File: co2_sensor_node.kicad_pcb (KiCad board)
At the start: 4 copper layers, 83 parts, among them J1 Conn_01x03, J10 Conn_01x05, J11 Conn_01x06_Male, J12 Conn_01x02, J13 TF-15x15, J2 Conn_01x03, J3 Conn_01x02, J4 Conn_01x02, J5 Conn_01x03, J6 Conn_01x03, J7 Conn_01x02, J8 Conn_01x03, J9 Conn_01x05, Q1 AO3400A, Q2 AO3401A, Q3 AO3401A, Q4 AO3400A, SW1 K2-1102SP-C4SC-04, U1 TPS62130, U2 ESP32-WROOM-32D, U3 TC1508S

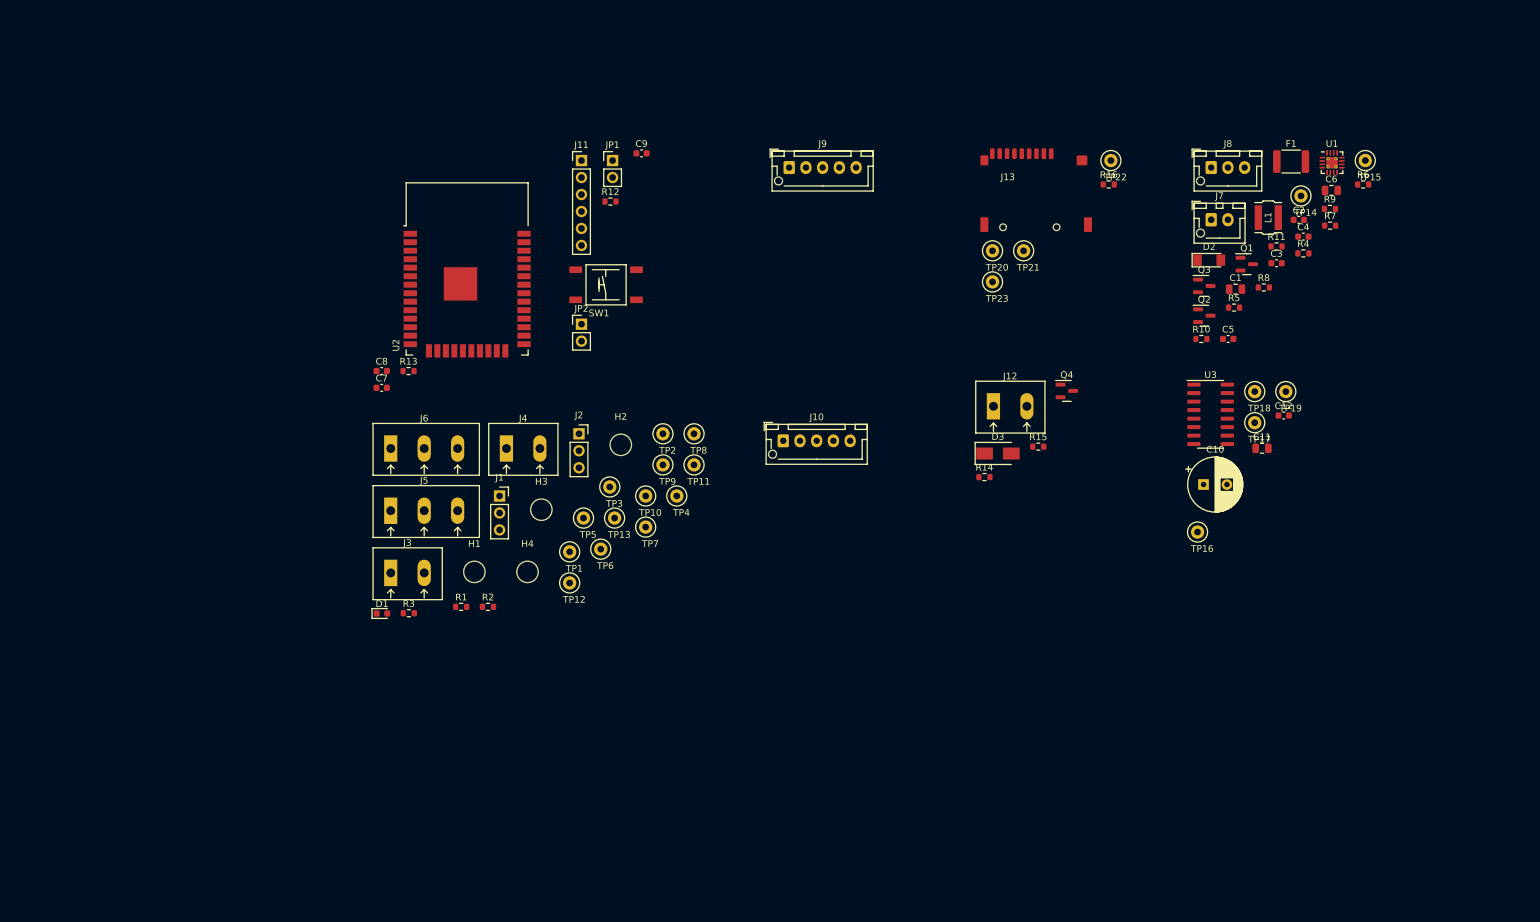
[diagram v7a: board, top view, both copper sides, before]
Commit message: Finish PCB layout
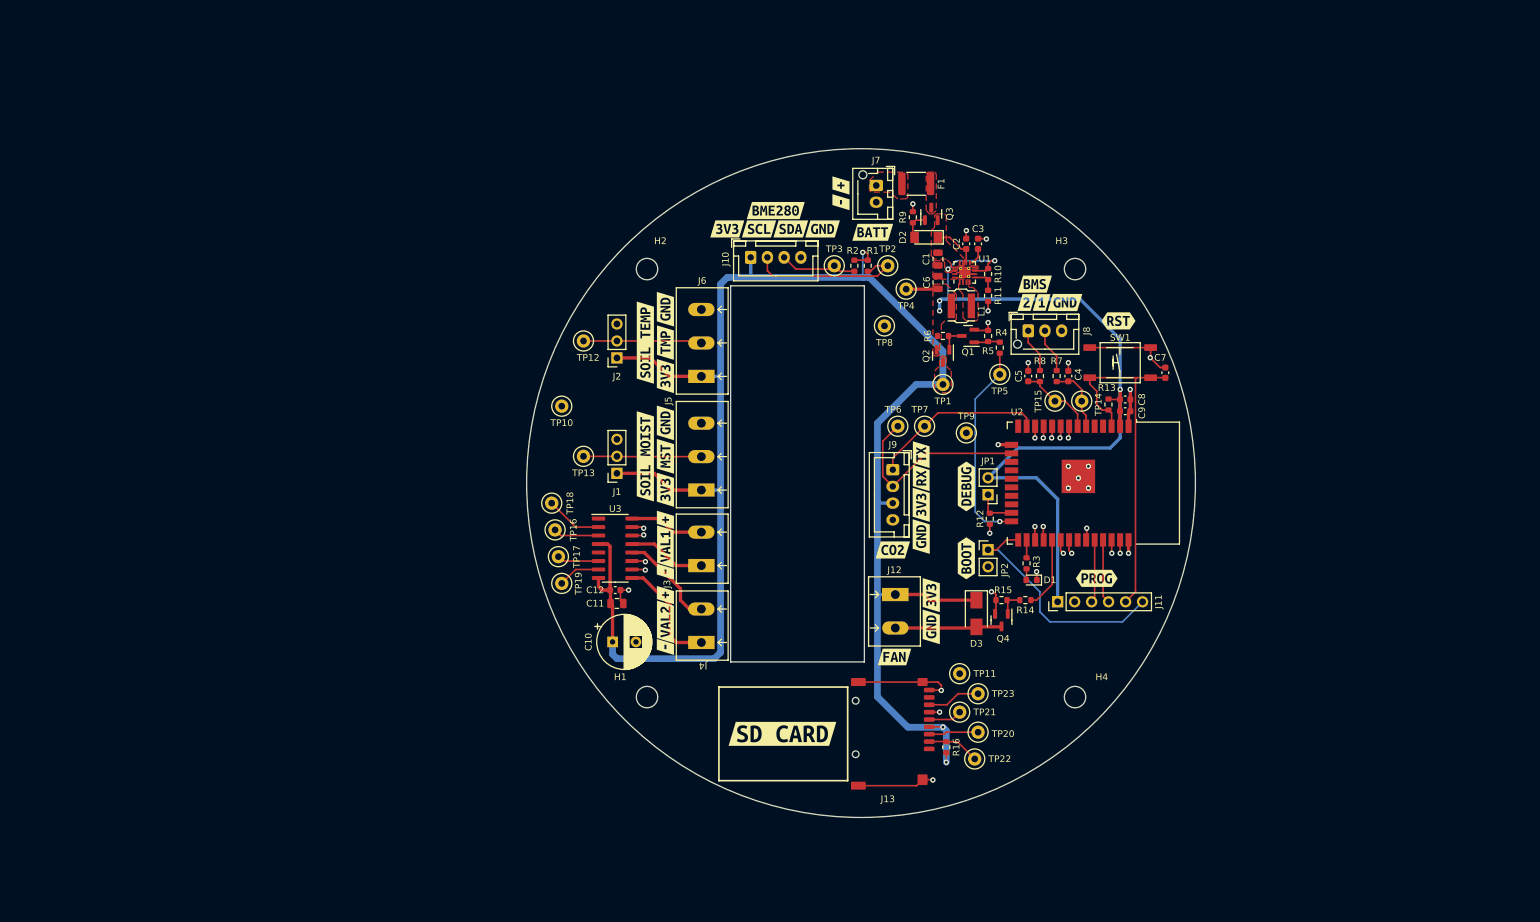
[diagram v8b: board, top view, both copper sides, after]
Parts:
- added kibuzzard-628CFF95: G***, kibuzzard-628CFF95, F.Cu at (121.2, 89.0)
- added kibuzzard-628CFF9F: G***, kibuzzard-628CFF9F, F.Cu at (121.2, 106.0)
- added kibuzzard-628CFFA6: G***, kibuzzard-628CFFA6, F.Cu at (121.2, 79.0)
- added kibuzzard-628CFFAE: G***, kibuzzard-628CFFAE, F.Cu at (121.2, 96.0)
- added kibuzzard-628CFFC0: G***, kibuzzard-628CFFC0, F.Cu at (121.2, 84.0)
- added kibuzzard-628CFFCE: G***, kibuzzard-628CFFCE, F.Cu at (121.2, 101.0)
- added kibuzzard-628D00BE: G***, kibuzzard-628D00BE, F.Cu at (138.8, 142.5)
- added kibuzzard-628D0108: G***, kibuzzard-628D0108, F.Cu at (155.5, 131.0)
- added kibuzzard-628D0116: G***, kibuzzard-628D0116, F.Cu at (161.0, 121.8)
- added kibuzzard-628D0120: G***, kibuzzard-628D0120, F.Cu at (161.0, 126.5)
- added kibuzzard-628D0190: G***, kibuzzard-628D0190, F.Cu at (189.0, 80.8)
- added kibuzzard-628D019E: G***, kibuzzard-628D019E, F.Cu at (185.8, 119.2)
- added kibuzzard-628D01AC: G***, kibuzzard-628D01AC, F.Cu at (166.2, 116.2)
- added kibuzzard-628D01D9: G***, kibuzzard-628D01D9, F.Cu at (166.2, 105.5)
- added kibuzzard-628D06EC: G***, kibuzzard-628D06EC, F.Cu at (152.2, 67.5)
- added kibuzzard-628D076D: G***, kibuzzard-628D076D, F.Cu at (121.2, 118.2)
- added kibuzzard-628D076D: G***, kibuzzard-628D076D, F.Cu at (147.5, 63.0)
- added kibuzzard-628D076D: G***, kibuzzard-628D076D, F.Cu at (121.2, 129.5)
- added kibuzzard-628D0781: G***, kibuzzard-628D0781, F.Cu at (121.2, 121.8)
- added kibuzzard-628D0781: G***, kibuzzard-628D0781, F.Cu at (147.5, 60.5)
- added kibuzzard-628D0781: G***, kibuzzard-628D0781, F.Cu at (121.2, 110.5)
- added kibuzzard-628D0804: G***, kibuzzard-628D0804, F.Cu at (159.5, 108.2)
- added kibuzzard-628D0814: G***, kibuzzard-628D0814, F.Cu at (159.5, 113.0)
- added kibuzzard-628D0827: G***, kibuzzard-628D0827, F.Cu at (159.5, 100.8)
- added kibuzzard-628D082D: G***, kibuzzard-628D082D, F.Cu at (159.5, 104.2)
- added kibuzzard-628D085C: G***, kibuzzard-628D085C, F.Cu at (155.2, 115.0)
- added kibuzzard-628D086F: G***, kibuzzard-628D086F, F.Cu at (118.2, 84.0)
- added kibuzzard-628D087A: G***, kibuzzard-628D087A, F.Cu at (118.2, 101.0)
- added kibuzzard-628D090E: G***, kibuzzard-628D090E, F.Cu at (130.5, 67.0)
- added kibuzzard-628D0915: G***, kibuzzard-628D0915, F.Cu at (144.8, 67.0)
- added kibuzzard-628D091C: G***, kibuzzard-628D091C, F.Cu at (140.0, 67.0)
- added kibuzzard-628D0922: G***, kibuzzard-628D0922, F.Cu at (135.2, 67.0)
- added kibuzzard-628D0934: G***, kibuzzard-628D0934, F.Cu at (137.8, 64.2)
- added kibuzzard-628E05D6: G***, kibuzzard-628E05D6, F.Cu at (176.5, 75.2)
- added kibuzzard-628E05DE: G***, kibuzzard-628E05DE, F.Cu at (181.0, 78.0)
- added kibuzzard-628E05E8: G***, kibuzzard-628E05E8, F.Cu at (177.5, 78.0)
- added kibuzzard-628E05EE: G***, kibuzzard-628E05EE, F.Cu at (175.2, 78.0)
- added kibuzzard-628E3C65: G***, kibuzzard-628E3C65, F.Cu at (121.2, 125.8)
- added kibuzzard-628E3C8D: G***, kibuzzard-628E3C8D, F.Cu at (121.2, 114.5)
- J10, J9: value Conn_01x05 -> Conn_01x04; footprint Connector_JST:JST_XH_B5B-XH-AM_1x05_P2.50mm_Vertical -> Connector_JST:JST_XH_B4B-XH-A_1x04_P2.50mm_Vertical
- moved C7 117.2 mm to (196.0, 88.5), turned to 90 degrees
- moved TP19 112.0 mm to (105.8, 120.0)
- moved C8 111.3 mm to (190.0, 92.5)
- moved TP18 106.4 mm to (104.2, 108.0)
- moved TP17 106.0 mm to (105.2, 116.0)
- moved R13 104.8 mm to (187.5, 93.2), turned to -90 degrees
- moved C12 103.3 mm to (113.8, 121.0)
- moved C11 99.2 mm to (114.0, 123.0)
- moved D1 97.3 mm to (176.0, 119.5), turned to 180 degrees
- moved J11 97.1 mm to (179.9, 122.8), turned to 90 degrees
- moved TP16 96.1 mm to (104.8, 112.0)
- moved U2 95.2 mm to (182.2, 105.0), turned to -90 degrees
- moved R3 92.7 mm to (175.2, 117.0), turned to 90 degrees
- moved TP22 91.8 mm to (167.5, 146.2)
- moved C10 91.4 mm to (113.3, 128.8)
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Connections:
- J3 pad 1: /Valve Driver/OUT_A -> /Valve Driver/OUT_B
- J3 pad 2: /Valve Driver/OUT_B -> /Valve Driver/OUT_A
- J4 pad 1: /Valve Driver/OUT_C -> /Valve Driver/OUT_D
- J4 pad 2: /Valve Driver/OUT_D -> /Valve Driver/OUT_C
- J9 pad 1: unconnected-(J9-Pad1) -> /CO2 Sensor Connector/UART_TX
- J9 pad 2: /CO2 Sensor Connector/UART_TX -> /CO2 Sensor Connector/UART_RX
- J9 pad 3: /CO2 Sensor Connector/UART_RX -> /Atmo sensor/3V3_IN
- J9 pad 4: /Atmo sensor/3V3_IN -> GND
- TP12 pad 1: unconnected-(TP12-Pad1) -> /Microprocessor section/TEMP_SENSOR
- U2 pad 11: /Microprocessor section/VALVE_2_REV -> /Microprocessor section/VALVE_2_FWD
- U2 pad 12: /Microprocessor section/VALVE_1_FWD -> /Microprocessor section/VALVE_2_REV
- U2 pad 8: /Microprocessor section/VALVE_1_REV -> /Microprocessor section/VALVE_1_FWD
- U2 pad 9: /Microprocessor section/VALVE_2_FWD -> /Microprocessor section/VALVE_1_REV
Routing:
- net /Atmo sensor/3V3_IN: track 0.00 -> 271.6 mm, vias 0 -> 3
- net /Microprocessor section/VALVE_2_REV: track 0.00 -> 141.7 mm, vias 0 -> 1
- net /Microprocessor section/VALVE_1_FWD: track 0.00 -> 140.6 mm, vias 0 -> 1
- net /Microprocessor section/VALVE_2_FWD: track 0.00 -> 140.3 mm, vias 0 -> 1
- net /Microprocessor section/VALVE_1_REV: track 0.00 -> 138.7 mm, vias 0 -> 1
- net /Microprocessor section/MOISTURE_SENSOR: track 0.00 -> 127.2 mm, vias 0 -> 1
- net +3V3: track 0.00 -> 124.4 mm, vias 0 -> 5
- net /Microprocessor section/TEMP_SENSOR: track 0.00 -> 118.9 mm, vias 0 -> 1
- net /Atmo sensor/SCL: track 0.00 -> 84.4 mm, vias 0 -> 1
- net GND: track 0.00 -> 81.3 mm, vias 0 -> 27
- net /Atmo sensor/SDA: track 0.00 -> 74.6 mm, vias 0 -> 1
- net /Microprocessor section/EN: track 0.00 -> 54.7 mm
- net /Microprocessor section/SPI_SD_CSN: track 0.00 -> 52.6 mm, vias 0 -> 1
- net /Microprocessor section/SPI_MOSI: track 0.00 -> 47.6 mm, vias 0 -> 1
- net /Microprocessor section/SPI_SCLK: track 0.00 -> 37.3 mm, vias 0 -> 1
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- added copper zone on F.Cu, net +3V3
- added copper zone on F.Cu, net +BATT
- added copper zone on F.Cu, net /Atmo sensor/3V3_IN
- added copper zone on F.Cu, net GND
- added copper zone on F.Cu, net Net-(F1-Pad1)
- added copper zone on F.Cu, net Net-(F1-Pad2)
- added copper zone on F.Cu, net Net-(L1-Pad1)
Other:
- board outline added: 100 x 100 mm
